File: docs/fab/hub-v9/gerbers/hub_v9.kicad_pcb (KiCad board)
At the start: 4 copper layers, 70 x 70 mm, 39 parts, among them U1 ESP32-S3-WROOM-1U-N8R8, U2 LoRa2021F33-2G4, U3 LoRa2021_Castellated, U4 SX1280, U5 MAX-M10S, U6 MS5611-01BA, U7 TPS7A02

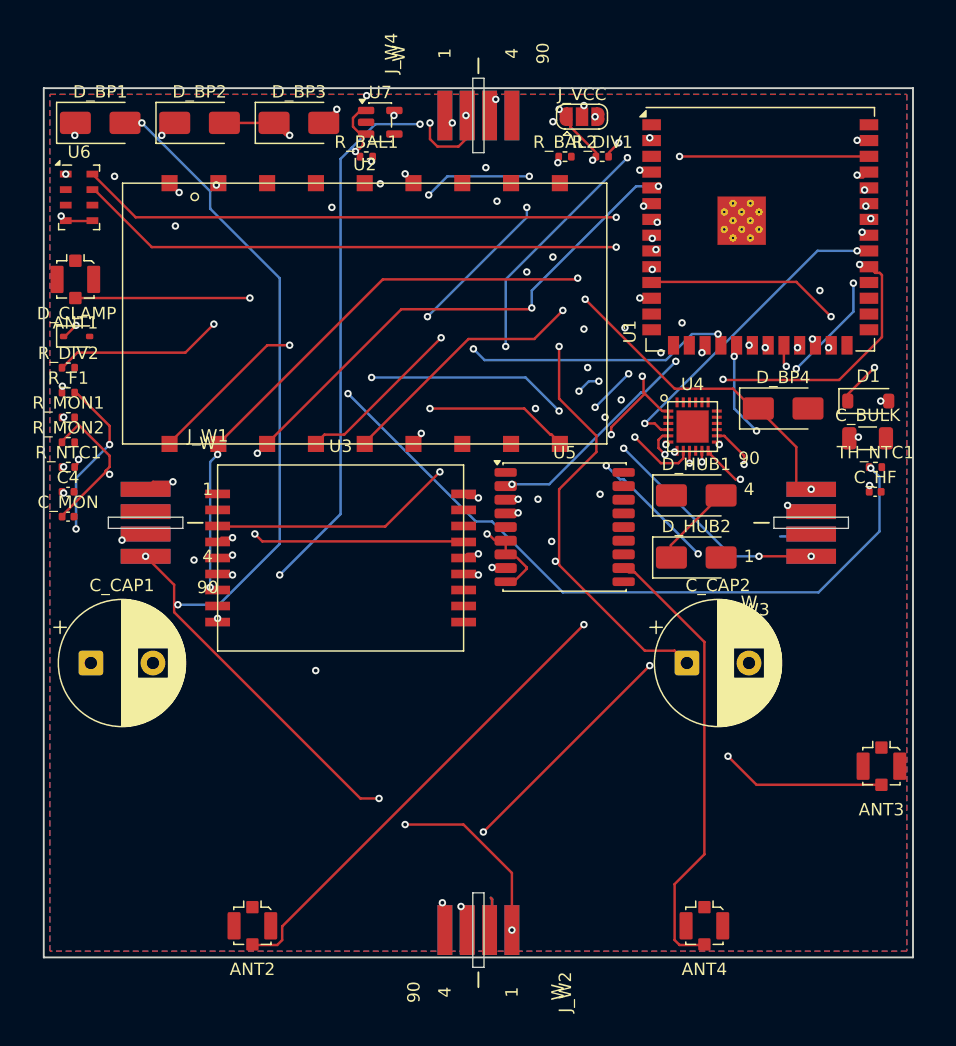
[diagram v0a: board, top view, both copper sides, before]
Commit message: fix(fab): REGENERATE the fab package -- it was missing 20 parts, including the whole RF chain
CLOSES test gate C2. The package at docs/fab/hub-v9/gerbers/ described a 39-footprint board while the
canonical board has 59. The 20 missing parts included C0, C1, C2, C3, C5, C6, C7, C8, C9, L1, L2 --
i.e. the ENTIRE SX1280 2.4 GHz matching and filter network. An order cut from that package would have
produced a board with no RF match. This is the same class as the H1 defect: the upload artefact did not
match the design, and nothing surfaced it.

VERIFIED: committed 59 footprints | packaged 59 footprints | missing 0.
test_netlist_integrity.py: 13 pass / 3 FAIL -> 14 pass / 2 FAIL (the 2 remaining are the base-station
F checks, queued next).

Regenerated with tracker/hardware/regen_fab_package.py, which plots the gerbers and drill from the
canonical board, copies the board into the package so C2 compares like-for-like, and writes a MANIFEST
carrying the SOURCE SHA256 (2dd363764b2314e8...) so provenance is provable rather than assumed. It
refuses to run if the canonical board has fewer footprints than the package, so a stale package cannot
be silently overwritten onto a current design.

Also written: hub_board_v9-bom-jlcpcb.csv (58 rows) and hub_board_v9-cpl-jlcpcb.csv (58 placements, DNP
and exclude-from-pos omitted), generated from the board's own footprint attributes rather than a
hand-kept list.

NOTE: the previous emitter, emit_jlc_files.py, writes BOM/CPL only and is hardcoded to a stale worktree
path (/home/.../worktrees/v9-route/...), so no script in the repo ever regenerated the package's BOARD
file. That is why it drifted.
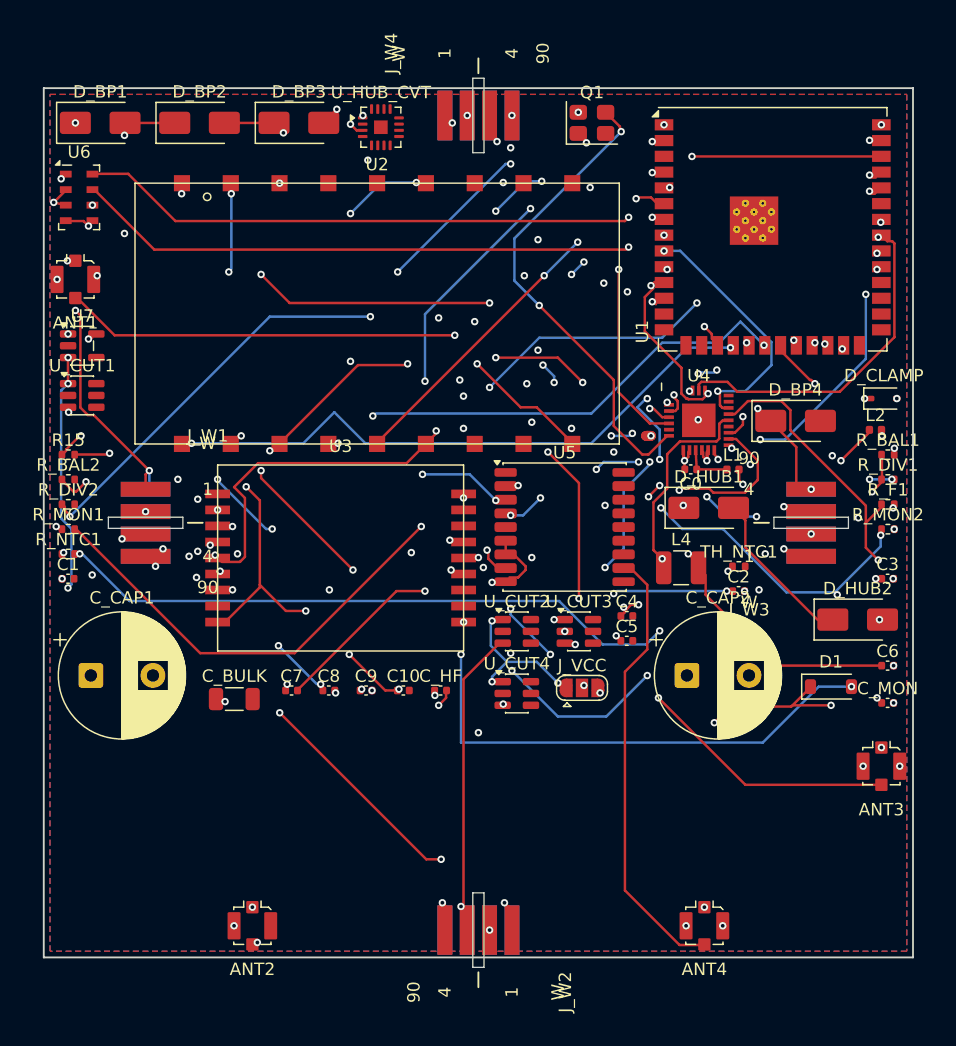
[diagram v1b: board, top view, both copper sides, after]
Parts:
- added C0: 0.8pF, Capacitor_SMD:C_0402_1005Metric, F.Cu at (52.1, 30.7)
- added C1: 1.2pF, Capacitor_SMD:C_0402_1005Metric, F.Cu at (1.96, 39.5)
- added C10: 100nF, Capacitor_SMD:C_0402_1005Metric, F.Cu at (29.0, 48.5)
- added C2: 1.2pF, Capacitor_SMD:C_0402_1005Metric, F.Cu at (56.0, 40.5)
- added C3: 100pF, Capacitor_SMD:C_0402_1005Metric, F.Cu at (68.0, 39.5)
- added C5: 10nF, Capacitor_SMD:C_0402_1005Metric, F.Cu at (47.0, 44.5)
- added C6: 10nF, Capacitor_SMD:C_0402_1005Metric, F.Cu at (68.0, 46.5)
- added C7: 0.5pF, Capacitor_SMD:C_0402_1005Metric, F.Cu at (20.0, 48.5)
- added C8: 100nF, Capacitor_SMD:C_0402_1005Metric, F.Cu at (23.0, 48.5)
- added C9: 470nF, Capacitor_SMD:C_0402_1005Metric, F.Cu at (26.0, 48.5)
- added L1: 3.0nH, Inductor_SMD:L_0402_1005Metric, F.Cu at (55.5, 30.7)
- added L2: 2.5nH, Inductor_SMD:L_0402_1005Metric, F.Cu at (67.0, 27.5)
- added L4: 15uH, Inductor_SMD:L_1210_3225Metric, F.Cu at (51.3, 38.6)
- added Q1: 52MHz, Crystal:Crystal_SMD_3225-4Pin_3.2x2.5mm, F.Cu at (44.1, 2.79)
- added R15: 0R, Resistor_SMD:R_0402_1005Metric, F.Cu at (1.98, 29.5)
- added U_CUT1: SN74LVC1G373DBVR, Package_TO_SOT_SMD:SOT-23-6, F.Cu at (3.10, 24.7)
- added U_CUT2: SN74LVC1G373DBVR, Package_TO_SOT_SMD:SOT-23-6, F.Cu at (38.1, 43.7)
- added U_CUT3: SN74LVC1G373DBVR, Package_TO_SOT_SMD:SOT-23-6, F.Cu at (43.1, 43.7)
- added U_CUT4: SN74LVC1G373DBVR, Package_TO_SOT_SMD:SOT-23-6, F.Cu at (38.1, 48.7)
- added U_HUB_CVT: BQ25504RGTR, Package_DFN_QFN:VQFN-16-1EP_3x3mm_P0.5mm_EP1.1x1.1mm, F.Cu at (27.1, 3.15)
- U4: footprint balloon_flight_v9:SX1280_QFN24 -> SX1280_QFN24
- moved C_MON 67.7 mm to (68.0, 49.5)
- moved R_F1 66.6 mm to (68.0, 33.5)
- moved R_MON2 66.4 mm to (68.0, 35.5)
- moved D_CLAMP 65.2 mm to (67.6, 25.0)
- moved C_BULK 55.2 mm to (15.3, 49.2)
- moved R_BAL1 48.4 mm to (68.0, 29.5)
- moved R_BAL2 47.7 mm to (1.98, 31.5)
- moved C4 46.1 mm to (47.0, 42.5)
- moved J_VCC 46.0 mm to (43.3, 48.3)
- moved C_HF 38.5 mm to (32.0, 48.5)
- moved R_DIV1 34.7 mm to (68.0, 31.5)
- moved U7 30.0 mm to (3.10, 20.7)
- moved D1 23.2 mm to (63.4, 48.2)
- moved D_HUB2 13.9 mm to (65.5, 42.8)
- moved TH_NTC1 13.6 mm to (56.0, 38.5)
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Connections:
- U1 pad 35: /SX1280_ANT_SW -> (no net)
- U4 pad 1: +3V3 -> /SX1280_VR_PA
- U4 pad 10: /SX1280_DIO1 -> /SX1280_DIO3
- U4 pad 11: /SX1280_DIO2 -> /SX1280_VBAT_IO
- U4 pad 12: /SX1280_DIO3 -> /SX1280_VDD
- U4 pad 13: /SX1280_ANT_SW -> GND
- U4 pad 14: /ANT2_2G4_RANGE -> /SX1280_DCC_SW
- U4 pad 15: GND -> +3V3
- U4 pad 16: GND -> /SX1280_MISO
- U4 pad 17: GND -> /SX1280_MOSI
- U4 pad 18: GND -> /SX1280_SCK
- U4 pad 19: GND -> /SX1280_CS_N
- U4 pad 2: +3V3 -> /SX1280_VDD
- U4 pad 22: GND -> /SX1280_RF
- U4 pad 3: GND -> /SX1280_RESET_N
- U4 pad 4: /SX1280_RESET_N -> /SX1280_XTA
- U4 pad 5: /SX1280_BUSY -> GND
- U4 pad 6: /SX1280_CS_N -> /SX1280_XTB
- U4 pad 7: /SX1280_SCK -> /SX1280_BUSY
- U4 pad 8: /SX1280_MOSI -> /SX1280_DIO1
- U4 pad 9: /SX1280_MISO -> /SX1280_DIO2
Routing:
- net /HUB_PV_N: track 0.00 -> 93.9 mm, vias 0 -> 6
- net /SX1280_VBAT_IO: track 0.00 -> 85.5 mm, vias 0 -> 8
- net /SX1280_RF_MATCH: track 0.00 -> 83.1 mm, vias 0 -> 7
- net /SX1280_VDD: track 0.00 -> 79.3 mm, vias 0 -> 7
- net /SX1280_RF_FILT: track 0.00 -> 65.7 mm, vias 0 -> 5
- net +3V3: track 159.8 -> 209.7 mm, vias 16 -> 15
- net /HUB_PV_P: track 0.00 -> 49.7 mm, vias 0 -> 5
- net /CUT_SENSE_W4: track 0.00 -> 47.7 mm, vias 1 -> 3
- net /F33_VCC: track 166.8 -> 125.3 mm, vias 8 -> 9
- net /SX1280_XTB: track 0.00 -> 38.4 mm, vias 0 -> 2
- net /SX1280_MISO: track 57.6 -> 20.5 mm, vias 6 -> 2
- net /F33_VSENSE: track 74.9 -> 108.8 mm, vias 4 -> 8
- net /SCAP_ADC: track 53.4 -> 85.2 mm, vias 4 -> 8
- net /SX1280_VR_PA: track 0.00 -> 30.1 mm, vias 0 -> 6
- net /SX1280_DIO1: track 0.00 -> 27.4 mm
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
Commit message: fix(fab): regenerate the order package -- the upload artefact did not match the board
WHY THIS MATTERS: the package in docs/fab/hub-v9/gerbers/ was cut from a board that is no longer the
board on master, so a fab upload from it would have shipped a different board than the one the gates
have been checking.

MEASURED BEFORE

    manifest source_sha256  2dd363764b2314e8c5f16db240fa979b4b20909afa521045df3eb0c857d8e4c5
    board on master         e55a294628fd38a73e5006fa7fa9138958ab986812b167263a9d130d661c93dd
                                                                              ^ DIFFERENT

The package was generated from the u4-rewire worktree. Since then the routed board was promoted to
canonical (the H1 fix) and U4's footprint ID was repaired (905b35272, on this branch), so the packaged
copy no longer corresponded to the canonical board.

MEASURED AFTER -- package and board are now the same bytes

    canonical board  : tracker/hardware/hub_board_v9.kicad_pcb  (59 footprints)
    packaged board   : docs/fab/hub-v9/gerbers/hub_v9.kicad_pcb (59 footprints)
    source_sha256    : e55a294628fd38a7...
    packaged copy    : e55a294628fd38a7...      identical
    gerbers rc=0, drill rc=0
    BOM 58 rows, CPL 58 placements

WHY 59 FOOTPRINTS GIVE 58 ORDERABLE PARTS -- checked, and it is correct

Exactly one footprint is absent from BOTH the BOM and the CPL:

    J_VCC   F33_VCC_SEL (5V raw | 3V3)   footprint SolderJumper-3_P1.3mm_Open_RoundedPad1.0x1.5mm

J_VCC is a SOLDER JUMPER: a pattern of exposed copper pads bridged by hand, not a component to purchase or
place. It is correctly excluded from both files, and its absence is design, not a defect. It selects the
F33's supply per ADR-047 (1=VSCAP, 2=COM, 3=+3V3).

GATES, RUN ON THE BOARD THE PACKAGE NOW MATCHES

    fab_readiness_guard --check   NOT ORDERABLE: 2 unrouted net(s), 0 accepted
                                  (/SX1280_MOSI and /SX1280_SCK each hold exactly ONE via and ZERO tracks)
    pad_audit        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
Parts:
- U4: footprint SX1280_QFN24 -> balloon_flight_v9:SX1280_QFN24
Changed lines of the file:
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@@
 		)
 	)
-	(footprint "SX1280_QFN24"
+	(footprint "balloon_flight_v9:SX1280_QFN24"
 		(layer "F.Cu")
 		(at 52.75 26.75)
@@
 		)
 		(embedded_fonts no)
+		(model "${KIPRJMOD}/3dmodels/hub/u4_sx1280_qfn24_envelope.wrl"
+			(offset
+				(xyz 0 0 0)
+			)
+			(scale
+				(xyz 1 1 1)
+			)
+			(rotate
+				(xyz 0 0 0)
+			)
+		)
 	)
 	(footprint "Package_DFN_QFN:VQFN-16-1EP_3x3mm_P0.5mm_EP1.1x1.1mm"
@@
 		)
 		(embedded_fonts no)
-		(model "${KICAD9_3DMODEL_DIR}/Package_DFN_QFN.3dshapes/VQFN-16-1EP_3x3mm_P0.5mm_EP1.1x1.1mm.step"
+		(model "${KIPRJMOD}/3dmodels/hub/u_hub_cvt_bq25504rgtr_envelope.wrl"
 			(offset
 				(xyz 0 0 0)

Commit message: fab: regenerate the fab package + u413 close-up from the stitched canonical board (ecd54b762)
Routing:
- net GND: vias 39 -> 42
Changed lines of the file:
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@@
+	)
+	(via
+		(at 35 43)
+		(size 0.6)
+		(drill 0.3)
+		(layers "F.Cu" "B.Cu")
+		(net 59)
 	)
 	(via
@@
 	)
 	(via
+		(at 33 44)
+		(size 0.6)
+		(drill 0.3)
+		(layers "F.Cu" "B.Cu")
+		(net 59)
+	)
+	(via
 		(at 49.95 2.95)
 		(size 0.6)
@@
 		(size 0.6)
 		(drill 0.3)
+		(layers "F.Cu" "B.Cu")
+		(net 59)
+	)
+	(via
+		(at 34 44)
+		(size 0.6)
+		(drill 0.3)

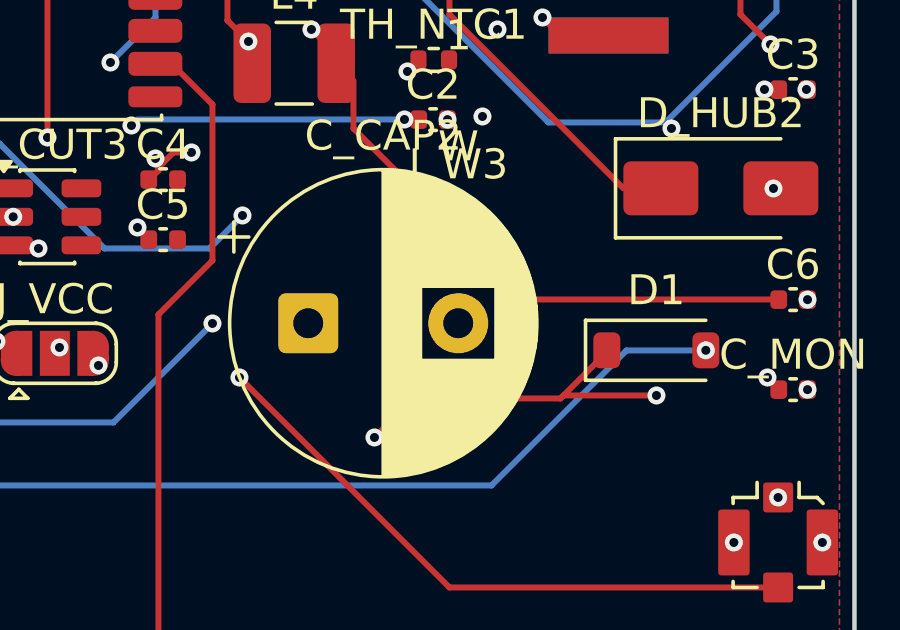
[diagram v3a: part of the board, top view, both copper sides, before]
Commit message: fab: regenerate package from the C_CAP2-fixed board (tracks 835, vias 288)
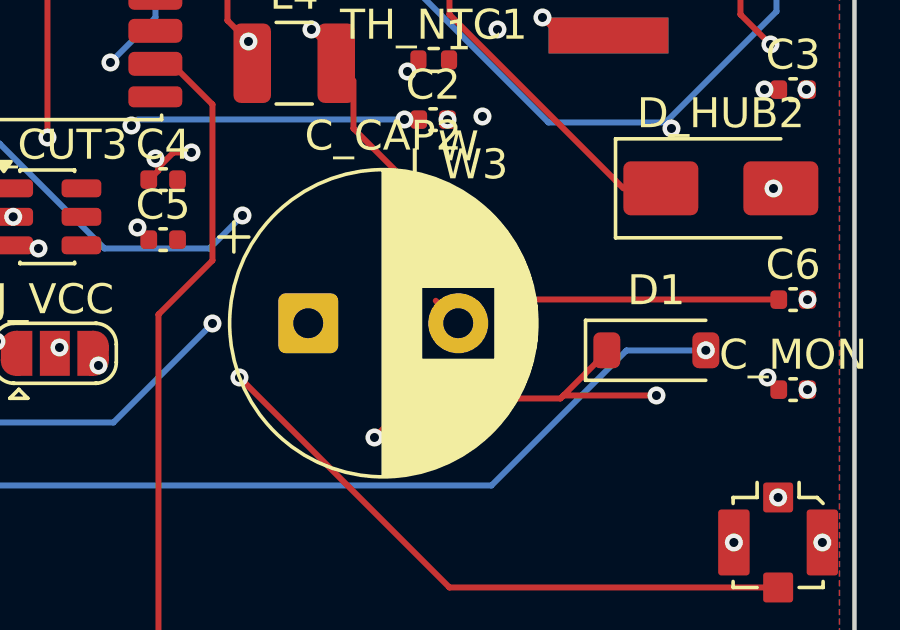
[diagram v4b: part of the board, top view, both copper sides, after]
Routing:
- net GND: track 16.0 -> 16.5 mm, vias 42 -> 41
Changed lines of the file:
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@@
+	)
+	(segment
+		(start 56.042967 46.542967)
+		(end 56.392967 46.892967)
+		(width 0.2)
+		(layer "F.Cu")
+		(net 59)
 	)
 	(segment
@@
 		(size 0.6)
 		(drill 0.3)
-		(layers "F.Cu" "B.Cu")
-		(net 59)
-	)
-	(via
-		(at 56.792502 47.292502)
-		(size 0.6)
-		(drill 0.3)

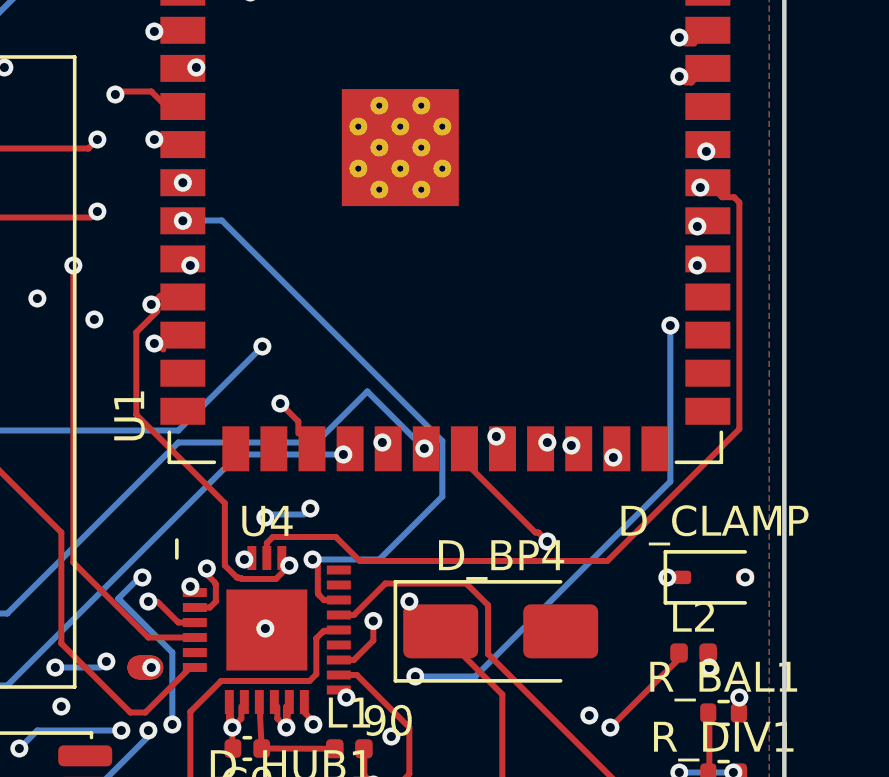
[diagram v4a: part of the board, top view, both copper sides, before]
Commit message: fab(package): regenerate after MOSI+SCK routing (embeds the new board)
The fab package embeds the canonical board (copied into docs/fab/hub-v9/gerbers/), so every
board change makes it stale. Regenerated from master f4c04aece (PR #245): gerbers, drill,
BOM (58 rows), CPL (58 placements), manifest.

PACKAGE SOURCE sha256: c3461fbc74349b7e...
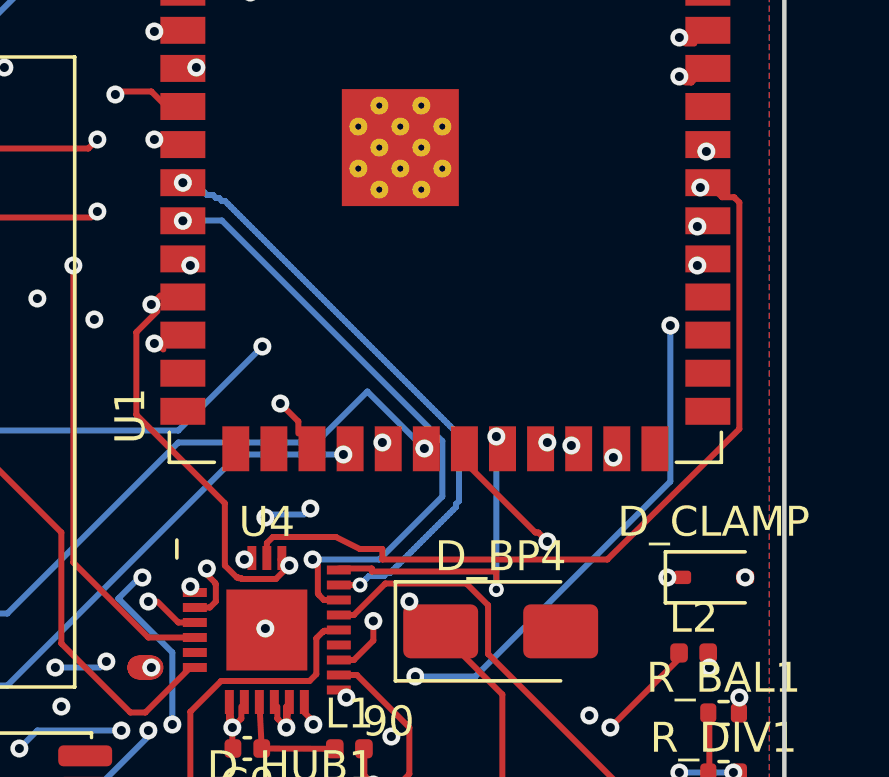
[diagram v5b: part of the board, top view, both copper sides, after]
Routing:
- net /SX1280_MOSI: track 0.00 -> 20.1 mm, vias 1 -> 2
- net /SX1280_SCK: track 0.00 -> 11.0 mm, vias 1 -> 2
